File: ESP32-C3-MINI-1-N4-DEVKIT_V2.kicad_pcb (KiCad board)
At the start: 2 copper layers, 19 parts, among them J1 USB_C_Receptacle_USB2.0, Q1 MMSS8050, SW1 TL6330AF200Q, U1 ESP32-C3-MINI-1, U2 CP2102N-Axx-xQFN28, U3 AZ1117CH-3.3TRG1

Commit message: started layout
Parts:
- added C10: 22pF, Capacitor_SMD:C_0603_1608Metric, F.Cu at (107.9, 27.5)
- added C11: 10uF, Capacitor_SMD:C_0805_2012Metric, F.Cu at (129.7, 47.7)
- added C12: 0.1uF, Capacitor_SMD:C_0603_1608Metric, F.Cu at (115.9, 22.1)
- added C13: 10uF, Capacitor_SMD:C_0805_2012Metric, F.Cu at (129.2, 22.2)
- added C14: 0.1uF, Capacitor_SMD:C_0603_1608Metric, F.Cu at (115.7, 53.4)
- added C15: 0.1uF, Capacitor_SMD:C_0603_1608Metric, F.Cu at (138.9, 104.7)
- added C16: 0.1uF, Capacitor_SMD:C_0603_1608Metric, F.Cu at (121.2, 104.8)
- added C6: 0.1uF, Capacitor_SMD:C_0603_1608Metric, F.Cu at (118.0, 88.9)
- added C7: 0.1uF, Capacitor_SMD:C_0603_1608Metric, F.Cu at (139.3, 79.7)
- added C8: 10uF, Capacitor_SMD:C_0805_2012Metric, F.Cu at (139.3, 83.4)
- added C9: 22pF, Capacitor_SMD:C_0603_1608Metric, F.Cu at (108.1, 22.4)
- added D3: SS1040, Diode_SMD:D_SOD-123, F.Cu at (127.4, 86.2)
- added D4: RX_LED, Diode_SMD:D_0603_1608Metric, F.Cu at (191.0, 38.5)
- added D5: TX_LED, Diode_SMD:D_0603_1608Metric, F.Cu at (198.3, 38.3)
- added J2: Conn_01x15, Connector_PinHeader_2.54mm:PinHeader_1x15_P2.54mm_Vertical, F.Cu at (55.8, 33.5)
- added J3: Conn_01x15, Connector_PinHeader_2.54mm:PinHeader_1x15_P2.54mm_Vertical, F.Cu at (64.6, 33.3)
- added Q2: MMSS8050, Package_TO_SOT_SMD:SOT-23, F.Cu at (156.6, 95.2)
- added R10: 0, Resistor_SMD:R_0603_1608Metric, F.Cu at (145.5, 22.3)
- added R11: 0, Resistor_SMD:R_0603_1608Metric, F.Cu at (145.4, 36.8)
- added R12: 0, Resistor_SMD:R_0603_1608Metric, F.Cu at (145.4, 31.7)
- added R13: 0, Resistor_SMD:R_0603_1608Metric, F.Cu at (145.3, 26.9)
- added R14: 1k, Resistor_SMD:R_0603_1608Metric, F.Cu at (191.1, 41.4)
- added R15: 1k, Resistor_SMD:R_0603_1608Metric, F.Cu at (198.5, 41.6)
- added R16: 4.7k, Resistor_SMD:R_0603_1608Metric, F.Cu at (160.1, 34.2)
- added R17: 4.7k, Resistor_SMD:R_0603_1608Metric, F.Cu at (160.3, 27.7)
- added R7: 4.7k, Resistor_SMD:R_0603_1608Metric, F.Cu at (118.0, 77.3)
- added R8: 10k, Resistor_SMD:R_0603_1608Metric, F.Cu at (151.6, 99.3)
- added R9: 10k, Resistor_SMD:R_0603_1608Metric, F.Cu at (151.3, 95.1)
- added SW2: TL6330AF200Q, Button_Switch_SMD:SW_Push_1P1T_NO_CK_KMR2, F.Cu at (138.9, 109.1)
- C1: value 22pF -> 1uF
- C2: value 0.1uF -> 1uF
- C3: value 1uF -> 10uF; footprint Capacitor_SMD:C_0603_1608Metric -> Capacitor_SMD:C_0805_2012Metric
- C4: value 4.7uF -> 0.1uF; footprint Capacitor_Tantalum_SMD:CP_EIA-3216-18_Kemet-A -> Capacitor_SMD:C_0603_1608Metric
- C5: footprint Capacitor_Tantalum_SMD:CP_EIA-3216-18_Kemet-A -> Capacitor_SMD:C_0805_2012Metric
- D1: value SS1040 -> PWR_LED; footprint Diode_SMD:D_SOD-123 -> Diode_SMD:D_0603_1608Metric
- R1: value 0 Ohm -> 10k
- R2: value 1k Ohm -> 1k
- R3: value 4.7k Ohm -> 10k
- R4: value 10k Ohm -> 10k
- R5: value 22.1k Ohm -> 22.1k
- R6: value 47.5k Ohm -> 47.5k
- U2: value CP2102N-Axx-xQFN28 -> CP2102N-Axx-xQFN24; footprint Package_DFN_QFN:QFN-28-1EP_5x5mm_P0.5mm_EP3.35x3.35mm -> Package_DFN_QFN:QFN-24-1EP_4x4mm_P0.5mm_EP2.6x2.6mm
- moved R5 63.7 mm to (176.1, 22.5)
- moved U1 57.9 mm to (87.3, 33.5)
- moved C1 54.9 mm to (123.7, 22.1)
- moved J1 53.3 mm to (129.9, 109.3)
- moved C3 51.6 mm to (129.2, 28.3)
- moved R6 50.8 mm to (176.0, 26.8)
- moved U2 50.5 mm to (127.2, 97.1)
- moved C2 48.0 mm to (123.4, 27.7)
- moved Q1 44.6 mm to (156.6, 99.8), turned to -90 degrees
- moved R1 44.3 mm to (167.9, 33.9)
- moved D2 43.2 mm to (126.3, 101.8), turned to -90 degrees
- moved SW1 41.3 mm to (121.1, 109.2), turned to -90 degrees
- moved C4 40.7 mm to (115.5, 60.0)
- moved R3 39.7 mm to (167.9, 23.1)
- moved R2 31.6 mm to (152.7, 34.1)
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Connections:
- C1 pad 1: unconnected-(C1-Pad1) -> /CHIP_PU
- C1 pad 2: unconnected-(C1-Pad2) -> Earth
- C2 pad 1: unconnected-(C2-Pad1) -> Net-(R5-Pad2)
- C2 pad 2: unconnected-(C2-Pad2) -> Earth
- C3 pad 1: unconnected-(C3-Pad1) -> VDD_3V3
- C3 pad 2: unconnected-(C3-Pad2) -> Earth
- C4 pad 1: unconnected-(C4-Pad1) -> VDD_3V3
- C4 pad 2: unconnected-(C4-Pad2) -> Earth
- C5 pad 1: unconnected-(C5-Pad1) -> VDD_5V
- C5 pad 2: unconnected-(C5-Pad2) -> Earth
- D1 pad 1: unconnected-(D1-Pad1) -> Earth
- D1 pad 2: unconnected-(D1-Pad2) -> Net-(D1-Pad2)
- D2 pad 1: unconnected-(D2-Pad1) -> Earth
- D2 pad 2: unconnected-(D2-Pad2) -> VBUS_5V
- D2 pad 3: unconnected-(D2-Pad3) -> /D-
- D2 pad 4: unconnected-(D2-Pad4) -> /D+
- J1 pad A1: Net-(J1-PadA1) -> Earth
- J1 pad A12: Net-(J1-PadA1) -> Earth
- J1 pad A4: Net-(J1-PadA4) -> VBUS_5V
- J1 pad A5: unconnected-(J1-PadA5) -> Net-(J1-PadA5)
- J1 pad A6: unconnected-(J1-PadA6) -> /D+
- J1 pad A7: unconnected-(J1-PadA7) -> /D-
- J1 pad A9: Net-(J1-PadA4) -> VBUS_5V
- J1 pad B1: Net-(J1-PadA1) -> Earth
- J1 pad B12: Net-(J1-PadA1) -> Earth
- J1 pad B4: Net-(J1-PadA4) -> VBUS_5V
- J1 pad B5: unconnected-(J1-PadB5) -> Net-(J1-PadB5)
- J1 pad B6: unconnected-(J1-PadB6) -> /D+
- J1 pad B7: unconnected-(J1-PadB7) -> /D-
- J1 pad B9: Net-(J1-PadA4) -> VBUS_5V
- J1 pad S1: unconnected-(J1-PadS1) -> Earth
- Q1 pad 1: unconnected-(Q1-Pad1) -> Net-(Q1-Pad1)
- Q1 pad 2: unconnected-(Q1-Pad2) -> /RTS
- Q1 pad 3: unconnected-(Q1-Pad3) -> /CHIP_PU
- R1 pad 1: unconnected-(R1-Pad1) -> VDD_3V3
- R1 pad 2: unconnected-(R1-Pad2) -> /CHIP_PU
- R2 pad 1: unconnected-(R2-Pad1) -> VDD_3V3
- R2 pad 2: unconnected-(R2-Pad2) -> Net-(R2-Pad2)
- R3 pad 1: unconnected-(R3-Pad1) -> VDD_3V3
- R3 pad 2: unconnected-(R3-Pad2) -> /GPIO8
- R4 pad 1: unconnected-(R4-Pad1) -> Net-(R4-Pad1)
- R4 pad 2: unconnected-(R4-Pad2) -> Earth
- R5 pad 1: unconnected-(R5-Pad1) -> VBUS_5V
- R5 pad 2: unconnected-(R5-Pad2) -> Net-(R5-Pad2)
- R6 pad 1: unconnected-(R6-Pad1) -> Net-(R5-Pad2)
- R6 pad 2: unconnected-(R6-Pad2) -> Earth
- SW1 pad 1: unconnected-(SW1-Pad1) -> Earth
- SW1 pad 3: (no net) -> /GPIO9
- SW1 pad 4: (no net) -> unconnected-(SW1-Pad4)
- U1 pad 1: unconnected-(U1-Pad1) -> Earth
- U1 pad 11: unconnected-(U1-Pad11) -> Earth
- U1 pad 12: unconnected-(U1-Pad12) -> /GPIO0
- U1 pad 13: unconnected-(U1-Pad13) -> /GPIO1
- U1 pad 14: unconnected-(U1-Pad14) -> Earth
- U1 pad 16: unconnected-(U1-Pad16) -> /GPIO10
- U1 pad 18: unconnected-(U1-Pad18) -> /GPIO4
- U1 pad 19: unconnected-(U1-Pad19) -> /GPIO5
- U1 pad 2: unconnected-(U1-Pad2) -> Earth
- U1 pad 20: unconnected-(U1-Pad20) -> /GPIO6
- U1 pad 21: unconnected-(U1-Pad21) -> /GPIO7
- U1 pad 22: unconnected-(U1-Pad22) -> /GPIO8
- U1 pad 23: unconnected-(U1-Pad23) -> /GPIO9
- U1 pad 26: unconnected-(U1-Pad26) -> /GPIO18
- U1 pad 27: unconnected-(U1-Pad27) -> /GPIO19
- U1 pad 3: unconnected-(U1-Pad3) -> VDD_3V3
- U1 pad 30: unconnected-(U1-Pad30) -> /U0RXD
- U1 pad 31: unconnected-(U1-Pad31) -> /U0TXD
- U1 pad 36: unconnected-(U1-Pad36) -> Earth
- U1 pad 5: unconnected-(U1-Pad5) -> /GPIO2
- U1 pad 6: unconnected-(U1-Pad6) -> /GPIO3
- U1 pad 8: unconnected-(U1-Pad8) -> /CHIP_PU
- U2 pad 13: unconnected-(U2-Pad13) -> Net-(D4-Pad1)
- U2 pad 14: unconnected-(U2-Pad14) -> Net-(D5-Pad1)
- U2 pad 15: unconnected-(U2-Pad15) -> Net-(R4-Pad1)
- U2 pad 19: unconnected-(U2-Pad19) -> /RTS
- U2 pad 2: unconnected-(U2-Pad2) -> Earth
- U2 pad 20: unconnected-(U2-Pad20) -> /U0TXD
- U2 pad 21: unconnected-(U2-Pad21) -> /U0RXD
- U2 pad 23: unconnected-(U2-Pad23) -> /DTR
- U2 pad 25: unconnected-(U2-Pad25) -> Earth
- U2 pad 3: Net-(U2-Pad29) -> /USB_DP
- U2 pad 4: unconnected-(U2-Pad4) -> /USB_DN
- U2 pad 5: unconnected-(U2-Pad5) -> VDD_3V3
- U2 pad 6: unconnected-(U2-Pad6) -> VDD_3V3
- U2 pad 7: unconnected-(U2-Pad7) -> VBUS_5V
- U2 pad 8: unconnected-(U2-Pad8) -> Net-(R5-Pad2)
- U2 pad 9: unconnected-(U2-Pad9) -> Net-(R2-Pad2)
- U3 pad 1: unconnected-(U3-Pad1) -> Earth
- U3 pad 2: unconnected-(U3-Pad2) -> VDD_3V3
- U3 pad 3: unconnected-(U3-Pad3) -> VDD_5V

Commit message: layout has begun
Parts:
- moved J3 151.1 mm to (215.3, 44.0)
- moved R10 103.6 mm to (125.1, 123.9)
- moved R5 98.8 mm to (107.9, 94.0), turned to 90 degrees
- moved R13 98.3 mm to (129.6, 123.9)
- moved C9 97.6 mm to (125.2, 118.5)
- moved C10 93.7 mm to (129.3, 118.7)
- moved R12 93.1 mm to (133.8, 124.1)
- moved D4 92.3 mm to (106.1, 74.7)
- moved D5 92.3 mm to (113.4, 74.5)
- moved R15 92.3 mm to (113.6, 77.8)
- moved R14 92.3 mm to (106.2, 77.6)
- moved R6 89.0 mm to (121.9, 97.5), turned to 90 degrees
- moved R11 87.7 mm to (138.3, 124.2)
- moved R17 80.3 mm to (148.3, 107.1)
- moved R4 78.2 mm to (107.9, 89.4), turned to 180 degrees
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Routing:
- net Earth: track 0.00 -> 62.7 mm, vias 0 -> 34
- net VBUS_5V: track 0.00 -> 27.8 mm, vias 0 -> 3
- net VDD_3V3: track 0.00 -> 10.8 mm, vias 0 -> 1
- net VDD_5V: track 0.00 -> 10.2 mm
- net /CHIP_PU: track 0.00 -> 8.67 mm, vias 0 -> 1
- net Net-(Q1-Pad1): track 0.00 -> 6.67 mm
- net /D+: track 0.00 -> 4.85 mm, vias 0 -> 1
- net /D-: track 0.00 -> 3.80 mm, vias 0 -> 1
- net /RTS: track 0.00 -> 3.62 mm
- net /GPIO9: track 0.00 -> 3.42 mm, vias 0 -> 1
- net /DTR: track 0.00 -> 1.91 mm
- net Net-(D1-Pad2): track 0.00 -> 1.70 mm
- net Net-(R5-Pad2): track 0.00 -> 1.63 mm
- net Net-(Q2-Pad1): track 0.00 -> 1.49 mm, vias 0 -> 1
- added copper zone on B.Cu, net Earth
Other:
- board outline added: 67.8 x 101.3 mm

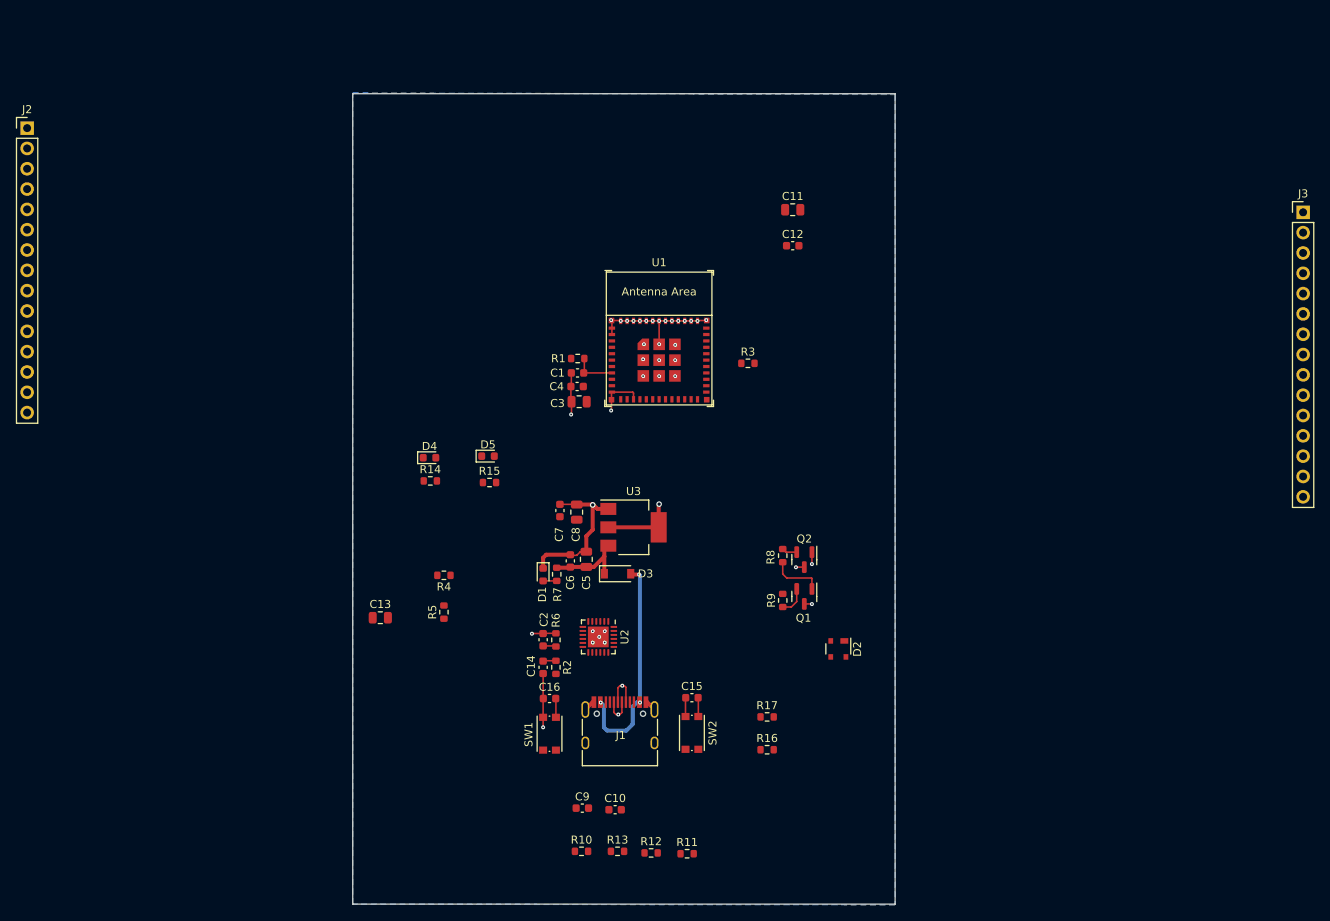
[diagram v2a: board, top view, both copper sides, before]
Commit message: layout finished, still need silkscreen
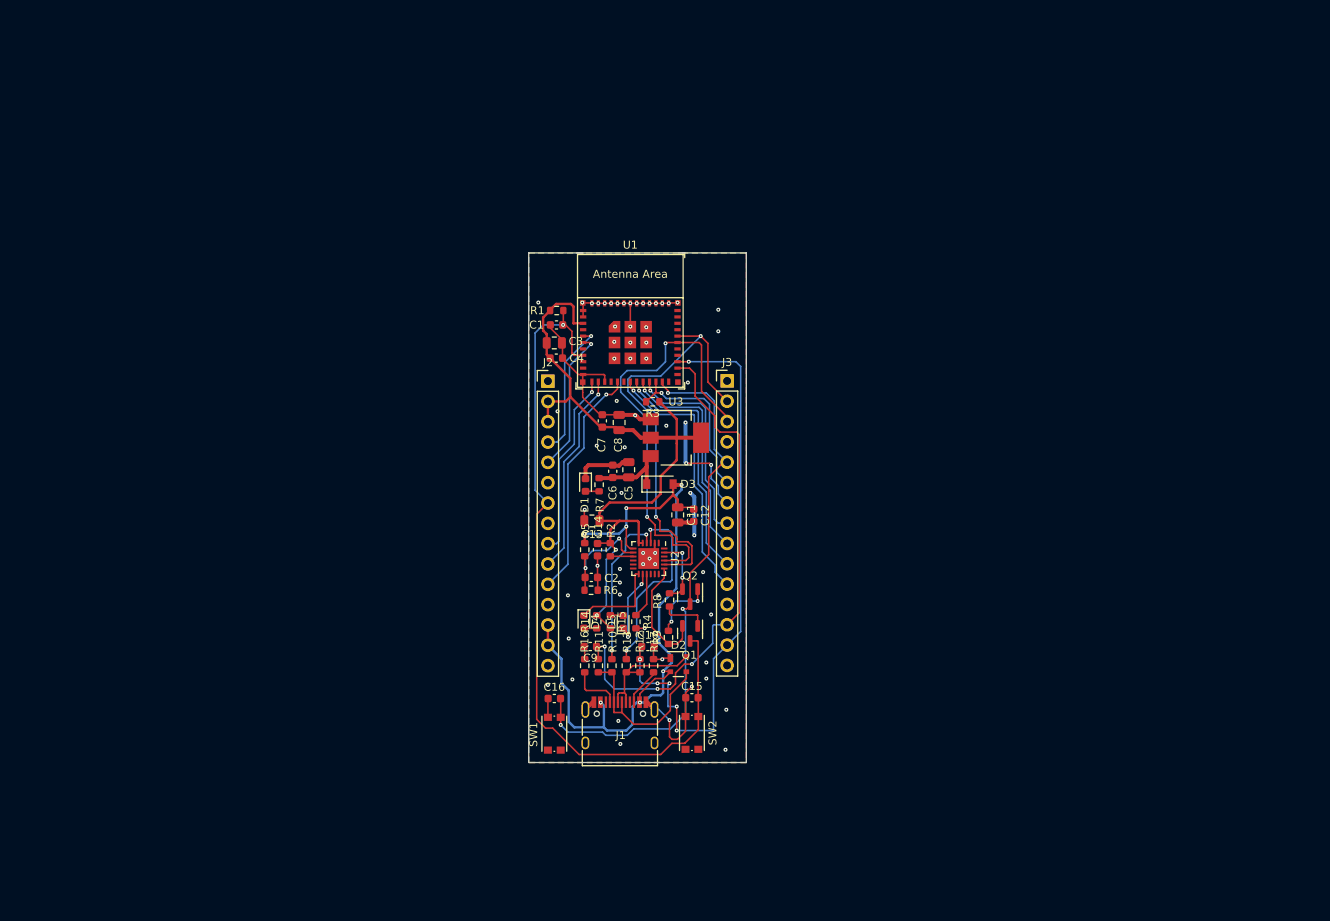
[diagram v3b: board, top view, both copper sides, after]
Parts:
- moved J3 75.0 mm to (143.3, 65.1)
- moved J2 72.4 mm to (120.9, 65.1)
- moved C11 40.8 mm to (137.1, 81.8), turned to -90 degrees
- moved C12 35.9 mm to (139.1, 81.9), turned to -90 degrees
- moved C13 29.1 mm to (126.4, 82.6), turned to 180 degrees
- moved D4 28.2 mm to (125.4, 95.2), turned to -90 degrees
- moved R14 27.3 mm to (127.0, 95.2), turned to 90 degrees
- moved D5 26.7 mm to (130.3, 95.2), turned to 90 degrees
- moved R11 26.0 mm to (127.2, 100.7), turned to 90 degrees
- moved R16 25.1 mm to (125.5, 100.7), turned to 90 degrees
- moved R4 24.7 mm to (131.9, 95.2), turned to -90 degrees
- moved R10 23.5 mm to (128.9, 100.7), turned to 90 degrees
- moved R12 23.4 mm to (132.4, 100.7), turned to 90 degrees
- moved R13 23.2 mm to (130.7, 100.7), turned to 90 degrees
- moved R15 23.0 mm to (128.7, 95.2), turned to -90 degrees
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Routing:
- net /CHIP_PU: track 8.67 -> 96.4 mm
- net VDD_3V3: track 10.8 -> 92.7 mm, vias 1 -> 2
- net /GPIO19: track 0.00 -> 74.9 mm, vias 0 -> 6
- net /GPIO9: track 3.42 -> 71.2 mm, vias 1 -> 3
- net /GPIO18: track 0.00 -> 66.0 mm, vias 0 -> 3
- net VBUS_5V: track 27.8 -> 92.4 mm, vias 3 -> 7
- net /U0RXD: track 0.00 -> 55.7 mm, vias 0 -> 2
- net /U0TXD: track 0.00 -> 55.2 mm, vias 0 -> 2
- net Earth: track 62.7 -> 102.3 mm, vias 34 -> 67
- net /GPIO4: track 0.00 -> 33.0 mm, vias 0 -> 1
- net /GPIO5: track 0.00 -> 30.0 mm, vias 0 -> 1
- net /GPIO10: track 0.00 -> 29.3 mm, vias 0 -> 1
- net /GPIO6: track 0.00 -> 27.4 mm, vias 0 -> 1
- net /GPIO1: track 0.00 -> 25.4 mm, vias 0 -> 1
- net /GPIO7: track 0.00 -> 25.1 mm, vias 0 -> 1
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- added copper zone on F.Cu, net Earth
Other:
- board size 67.8 x 101.3 mm -> 27.2 x 63.7 mm

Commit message: submitted to jlcpcb
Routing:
- net Earth: track 102.3 -> 111.2 mm
- net Net-(R5-Pad2): track 14.0 -> 12.8 mm
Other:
- board size 27.2 x 63.7 mm -> 27.2 x 63.8 mm
- board text added: "0"
- board text added: "1"
- board text added: "10"
- board text added: "18"
- board text added: "19"
- board text added: "2"
- board text added: "3"
- board text added: "3V3"
- board text added: "4"
- board text added: "5"
- board text added: "5V"
- board text added: "6"
- board text added: "7"
- board text added: "8"
- board text added: "9"
- board text added: "D T R"
- board text added: "EN"
- board text added: "G"
- board text added: "R T S"
- board text added: "U0RXD"
- board text added: "U0TXD"
